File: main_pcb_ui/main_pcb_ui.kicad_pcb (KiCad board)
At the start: 2 copper layers, 74 x 24 mm, 11 parts, among them J1 Conn_02x02_Odd_Even, J2 Conn_02x02_Odd_Even, J3 Conn_02x02_Odd_Even, J4 Conn_02x02_Odd_Even, SW1 SP+, SW2 SP-, SW3 TRIG, SW4 BR+, SW5 BR-

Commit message: Routed and updated UI board
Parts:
- added R2: 1k, Resistor_SMD:R_0603_1608Metric, F.Cu at (122.0, 94.0)
- added R3: 1k, Resistor_SMD:R_0603_1608Metric, F.Cu at (122.0, 106.0)
- added R4: 1k, Resistor_SMD:R_0603_1608Metric, F.Cu at (147.0, 106.0)
- added R5: 1k, Resistor_SMD:R_0603_1608Metric, F.Cu at (158.0, 94.0)
- added R6: 1k, Resistor_SMD:R_0603_1608Metric, F.Cu at (158.0, 105.0)
- J1, J2, J3, J4: footprint Connector_PinHeader_2.54mm:PinHeader_2x02_P2.54mm_Vertical -> Connector_PinSocket_2.54mm:PinSocket_2x02_P2.54mm_Vertical
- R1: value R -> 220
- moved J1 2.54 mm to (105.7, 106.7), turned to 180 degrees
- moved J2 2.54 mm to (105.7, 90.7), turned to 180 degrees
- moved J3 2.54 mm to (171.7, 90.7), turned to 180 degrees
- moved J4 2.54 mm to (171.7, 106.7), turned to 180 degrees
- moved R1 0.80 mm to (145.0, 92.0)
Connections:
- J1 pad 2: /TRIG -> /SP-
- J1 pad 4: GND -> /TRIG
- J2 pad 1: GND -> +3V3
- J2 pad 4: /SP- -> GND
- J3 pad 3: /BR- -> /LED
- J4 pad 1: /LED -> /BR-
- SW1 pad 2: /SP+ -> GND
- SW2 pad 2: /SP- -> GND
- SW3 pad 2: /TRIG -> GND
- SW4 pad 2: /BR+ -> GND
- SW5 pad 2: /BR- -> GND
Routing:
- net +3V3: track 0.00 -> 89.6 mm
- net /TRIG: track 0.00 -> 39.5 mm
- net /LED: track 0.00 -> 30.9 mm
- net /SP+: track 0.00 -> 15.8 mm
- net /BR+: track 0.00 -> 15.8 mm
- net /BR-: track 0.00 -> 13.6 mm
- net /SP-: track 0.00 -> 13.4 mm
- net Net-(D1-Pad2): track 0.00 -> 2.91 mm
- added copper zone on B.Cu, net GND
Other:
- board text added: "Brightn+"
- board text added: "Brightn-"
- board text added: "STATUS"
- board text added: "Speed+"
- board text added: "Speed-"
- board text added: "TRIG"

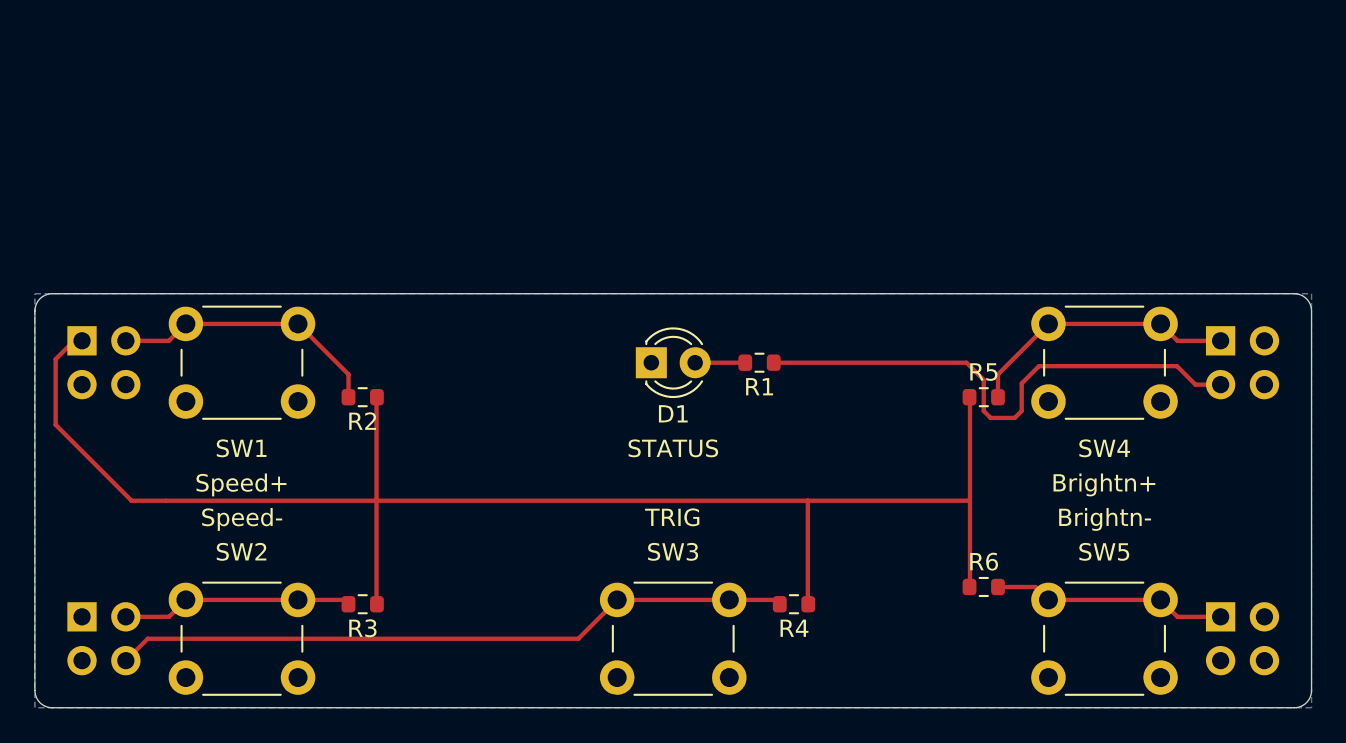
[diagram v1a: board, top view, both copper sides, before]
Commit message: Added power button to ui, increased size of board, and moved connectors 15 mm up
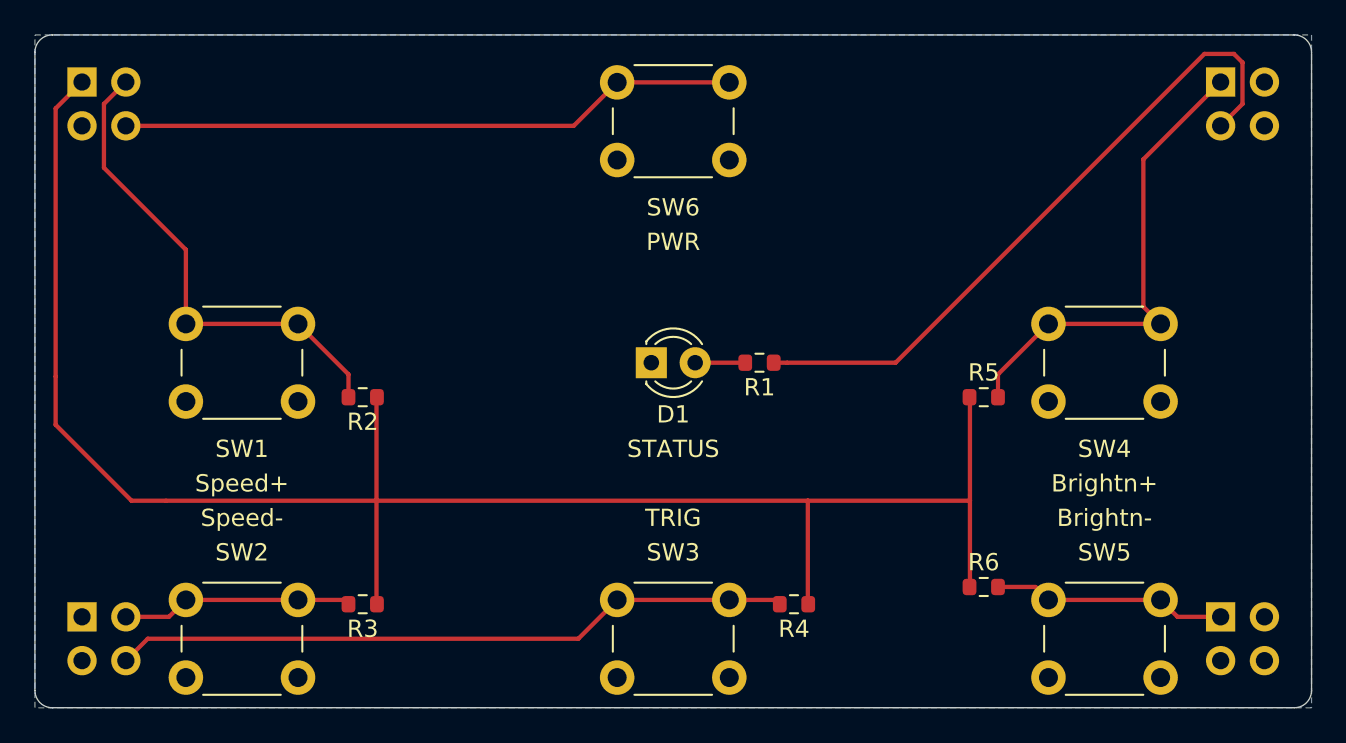
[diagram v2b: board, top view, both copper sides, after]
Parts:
- added SW6: SP+, Button_Switch_THT:SW_PUSH_6mm_H8mm, F.Cu at (136.8, 75.8)
- moved J2 15.0 mm to (105.7, 75.7)
- moved J3 15.0 mm to (171.7, 75.7)
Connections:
- J2 pad 4: GND -> /MASTER_ON
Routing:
- net /MASTER_ON: track 0.00 -> 36.0 mm
- net +3V3: track 89.6 -> 104.4 mm
- net /SP+: track 15.8 -> 28.5 mm
- net /BR+: track 15.8 -> 28.3 mm
- net /LED: track 30.9 -> 39.0 mm
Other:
- board size 74 x 24 mm -> 74 x 39 mm
- board text added: "PWR"

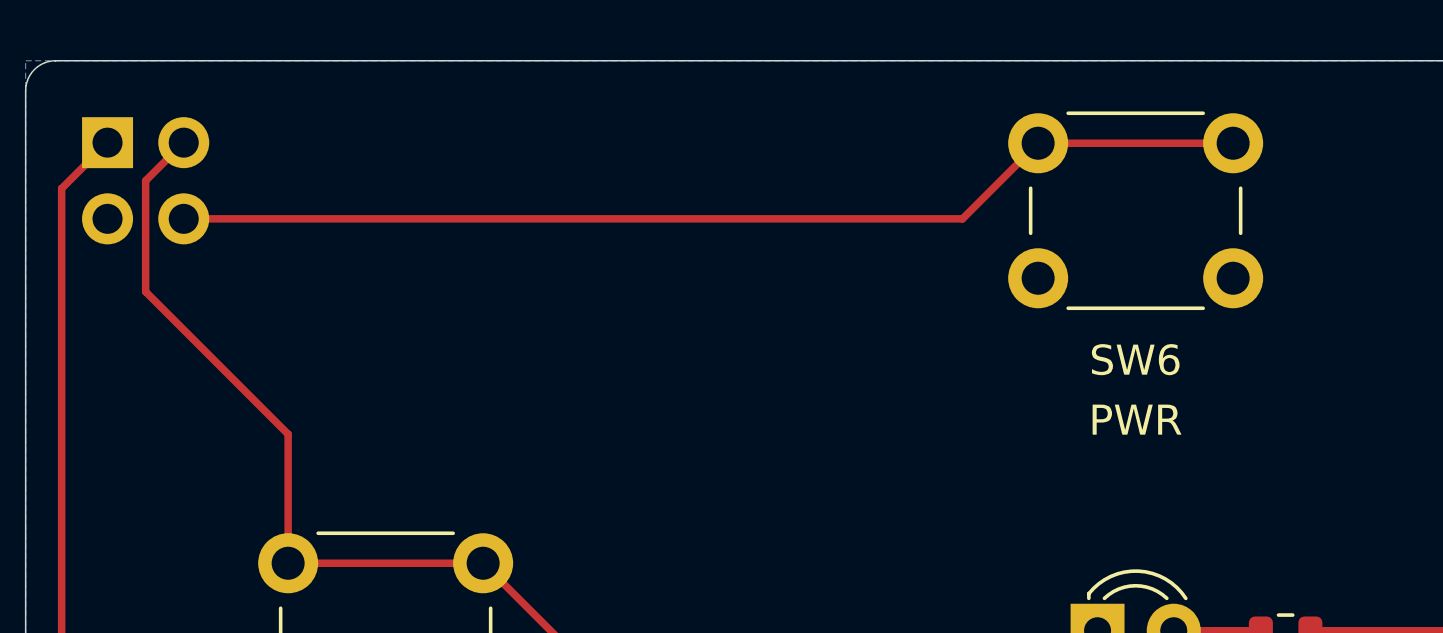
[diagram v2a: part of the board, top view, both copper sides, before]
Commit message: Corrected position of power button
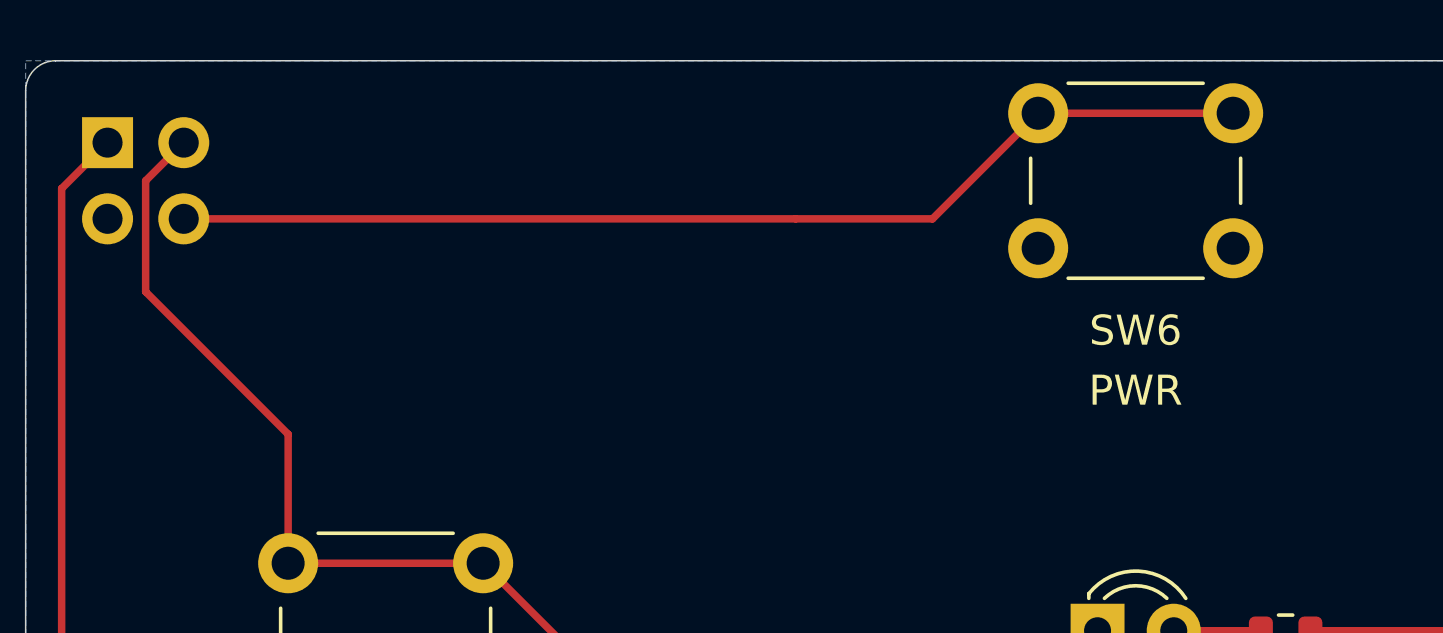
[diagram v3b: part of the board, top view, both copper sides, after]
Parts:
- moved SW6 1.00 mm to (136.8, 74.8)

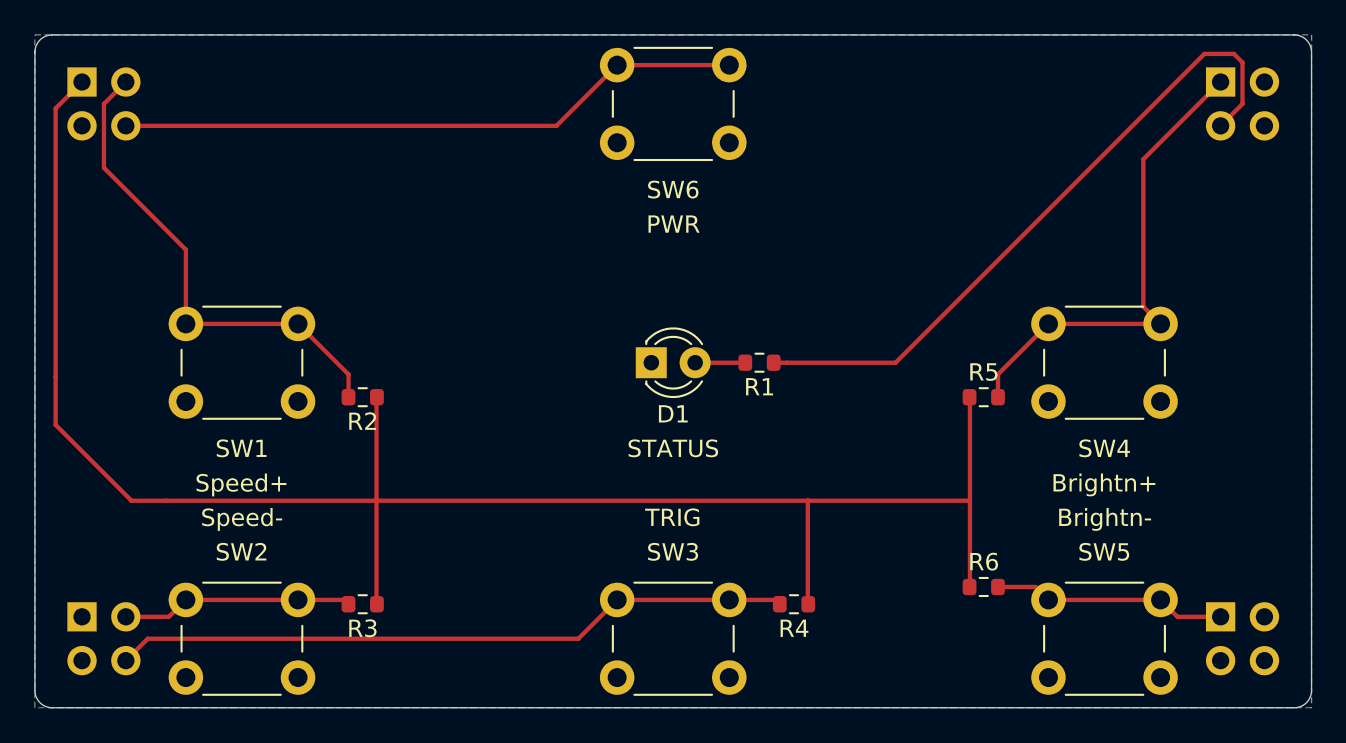
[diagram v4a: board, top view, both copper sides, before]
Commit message: Merged PCBs to KiCAD 6 format
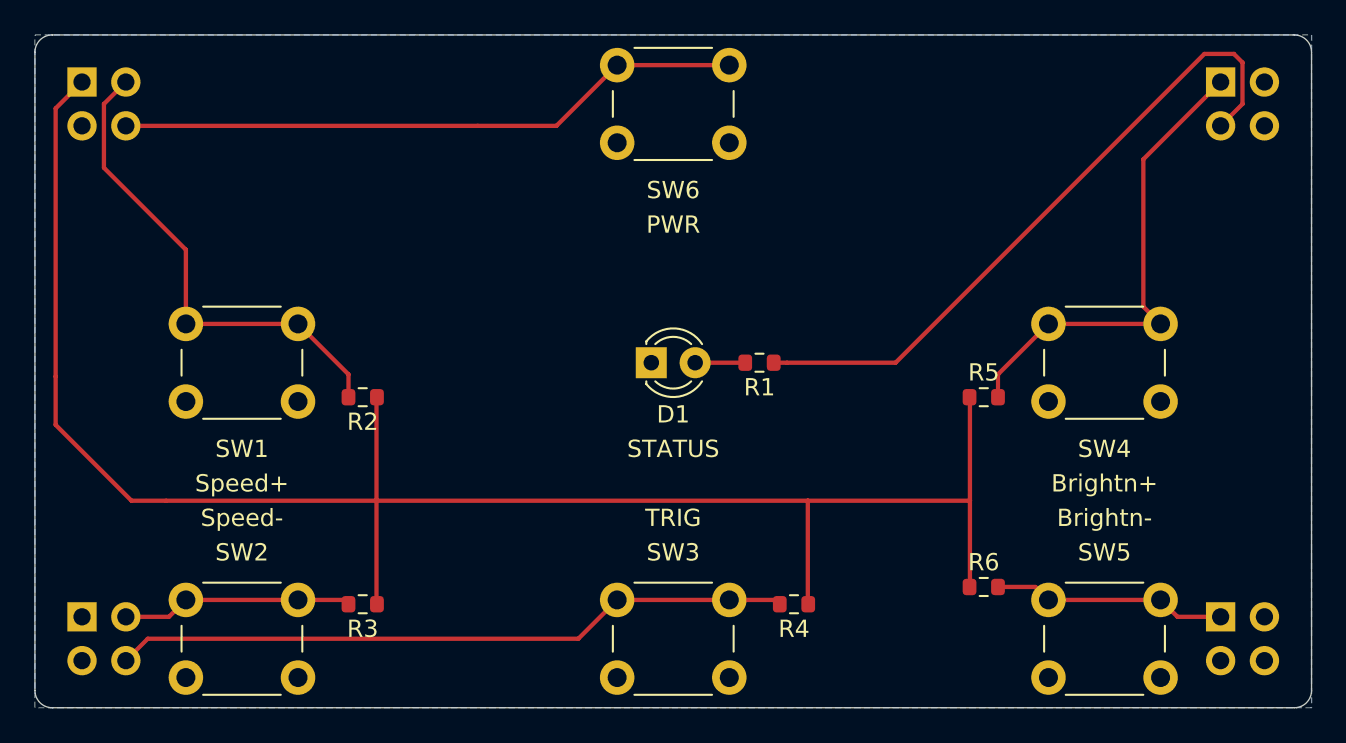
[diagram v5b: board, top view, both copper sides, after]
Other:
- net class Default removed
